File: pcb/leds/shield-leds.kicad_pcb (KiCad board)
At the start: 8 copper layers, 50 x 50 mm, 406 parts, among them J1 QSH-060-01-L-D-A, J2 QSH-060-01-L-D-A, J3 QTH-060-01-L-D-A, J4 QTH-060-01-L-D-A

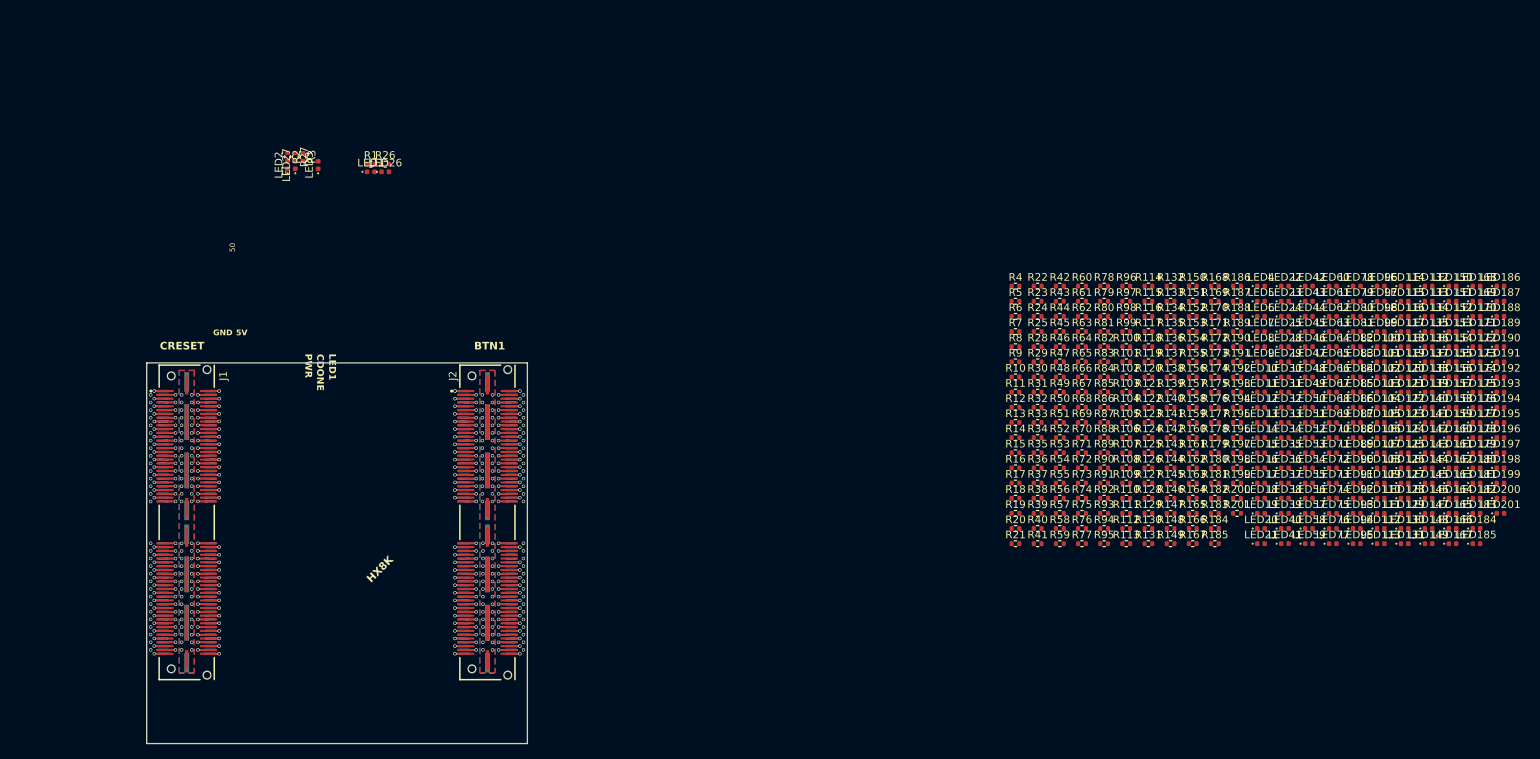
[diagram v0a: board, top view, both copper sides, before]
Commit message: [pcb][leds] left side routed
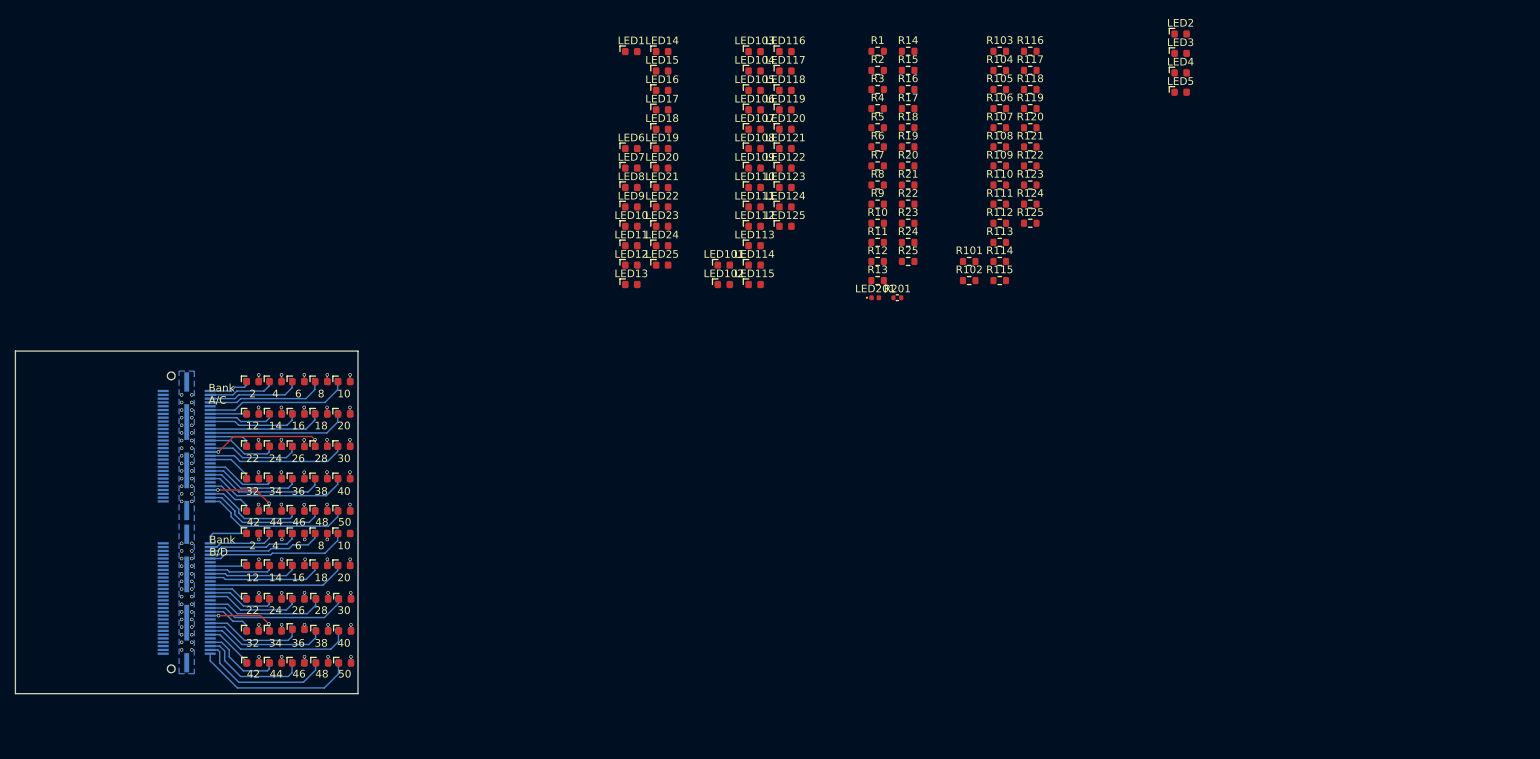
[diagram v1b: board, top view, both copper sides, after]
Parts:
- removed the J1 at (41.8, 81.1)
- removed J2: QSH-060-01-L-D-A, !Misc:SAMTEC_QSH-060-01-X-D-A
- removed J4: QTH-060-01-L-D-A, !Misc:SAMTEC_QTH-060-01-X-D-A
- removed LED100, LED151, LED152, LED153, LED154, LED155, LED156, LED157, LED158, LED159, LED160, LED161, LED162, LED163, LED164, LED165, LED166, LED167, LED168, LED169, LED170, LED171, LED172, LED173, LED174, LED175, LED176, LED177, LED178, LED179, LED180, LED181, LED182, LED183, LED184, LED185, LED186, LED187, LED188, LED189, LED190, LED191, LED192, LED193, LED194, LED195, LED196, LED197, LED198, LED199, LED200, LED51, LED52, LED53, LED54, LED55, LED56, LED57, LED58, LED59, LED60, LED61, LED62, LED63, LED64, LED65, LED66, LED67, LED68, LED69, LED70, LED71, LED72, LED73, LED74, LED75, LED76, LED77, LED78, LED79, LED80, LED81, LED82, LED83, LED84, LED85, LED86, LED87, LED88, LED89, LED90, LED91, LED92, LED93, LED94, LED95, LED96, LED97, LED98, LED99: Blue, Diode_SMD:D_0402_1005Metric
- removed R100, R151, R152, R153, R154, R155, R156, R157, R158, R159, R160, R161, R162, R163, R164, R165, R166, R167, R168, R169, R170, R171, R172, R173, R174, R175, R176, R177, R178, R179, R180, R181, R182, R183, R184, R185, R186, R187, R188, R189, R190, R191, R192, R193, R194, R195, R196, R197, R198, R199, R200, R51, R52, R53, R54, R55, R56, R57, R58, R59, R60, R61, R62, R63, R64, R65, R66, R67, R68, R69, R70, R71, R72, R73, R74, R75, R76, R77, R78, R79, R80, R81, R82, R83, R84, R85, R86, R87, R88, R89, R90, R91, R92, R93, R94, R95, R96, R97, R98, R99: 2.2k, Resistor_SMD:R_0402_1005Metric
- LED1, LED10, LED101, LED102, LED103, LED104, LED105, LED106, LED107, LED108, LED109, LED11, LED110, LED111, LED112, LED113, LED114, LED115, LED116, LED117, LED118, LED119, LED12, LED120, LED121, LED122, LED123, LED124, LED125, LED126, LED127, LED128, LED129, LED13, LED130, LED131, LED132, LED133, LED134, LED135, LED136, LED137, LED138, LED139, LED14, LED140, LED141, LED142, LED143, LED144, LED145, LED146, LED147, LED148, LED149, LED15, LED150, LED16, LED17, LED18, LED19, LED2, LED20, LED21, LED22, LED23, LED24, LED25, LED26, LED27, LED28, LED29, LED3, LED30, LED31, LED32, LED33, LED34, LED35, LED36, LED37, LED38, LED39, LED4, LED40, LED41, LED42, LED43, LED44, LED45, LED46, LED47, LED48, LED49, LED5, LED50, LED6, LED7, LED8, LED9: footprint Diode_SMD:D_0402_1005Metric -> !Misc:D_0603_1608Metric
- R1, R10, R101, R102, R103, R104, R105, R106, R107, R108, R109, R11, R110, R111, R112, R113, R114, R115, R116, R117, R118, R119, R12, R120, R121, R122, R123, R124, R125, R13, R14, R15, R16, R17, R18, R19, R2, R20, R21, R22, R23, R24, R25, R3, R4, R5, R6, R7, R8, R9: footprint Resistor_SMD:R_0402_1005Metric -> Resistor_SMD:R_0603_1608Metric
- R126, R127, R128, R129, R130, R131, R132, R133, R134, R135, R136, R137, R138, R139, R140, R141, R142, R143, R144, R145, R146, R147, R148, R149, R150, R26, R27, R28, R29, R30, R31, R32, R33, R34, R35, R36, R37, R38, R39, R40, R41, R42, R43, R44, R45, R46, R47, R48, R49, R50: footprint Resistor_SMD:R_0402_1005Metric -> Resistor_SMD:R_0603_1608Metric; moved to B.Cu
- moved LED136 158.0 mm to (50.5, 91.2)
- moved LED141 156.9 mm to (50.5, 95.4)
- moved LED146 155.9 mm to (50.5, 99.6)
- moved LED132 155.8 mm to (53.5, 86.8)
- moved LED137 154.6 mm to (53.5, 91.2)
- moved LED150 153.7 mm to (62.6, 99.6)
- moved LED142 153.6 mm to (53.5, 95.4)
- moved LED147 152.7 mm to (53.5, 99.6)
- moved LED133 152.4 mm to (56.5, 86.8)
- moved LED126 151.6 mm to (50.4, 82.5)
- moved LED131 151.3 mm to (50.5, 86.8)
- moved LED138 151.3 mm to (56.5, 91.2)
- moved LED143 150.2 mm to (56.5, 95.1)
- moved LED148 149.5 mm to (56.4, 99.6)
- moved LED134 149.1 mm to (59.5, 86.8)
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- renumbered J3 to J1
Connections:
- R101 pad 1: C1 -> B1
- R102 pad 1: C3 -> B3
- R103 pad 1: C5 -> B5
- R104 pad 1: C7 -> B7
- R105 pad 1: C9 -> B9
- R106 pad 1: C11 -> B11
- R107 pad 1: C13 -> B13
- R108 pad 1: C15 -> B15
- R109 pad 1: C17 -> B17
- R110 pad 1: C19 -> B19
- R111 pad 1: C21 -> B21
- R112 pad 1: C23 -> B23
- R113 pad 1: C25 -> B25
- R114 pad 1: C27 -> B27
- R115 pad 1: C29 -> B29
- R116 pad 1: C31 -> B31
- R117 pad 1: C33 -> B33
- R118 pad 1: C35 -> B35
- R119 pad 1: C37 -> B37
- R120 pad 1: C39 -> B39
- R121 pad 1: C41 -> B41
- R122 pad 1: C43 -> B43
- R123 pad 1: C45 -> B45
- R124 pad 1: C47 -> B47
- R125 pad 1: C49 -> B49
- R126 pad 1: C2 -> B2
- R127 pad 1: C4 -> B4
- R128 pad 1: C6 -> B6
- R129 pad 1: C8 -> B8
- R130 pad 1: C10 -> B10
- R131 pad 1: C12 -> B12
- R132 pad 1: C14 -> B14
- R133 pad 1: C16 -> B16
- R134 pad 1: C18 -> B18
- R135 pad 1: C20 -> B20
- R136 pad 1: C22 -> B22
- R137 pad 1: C24 -> B24
- R138 pad 1: C26 -> B26
- R139 pad 1: C28 -> B28
- R140 pad 1: C30 -> B30
- R141 pad 1: C32 -> B32
- R142 pad 1: C34 -> B34
- R143 pad 1: C36 -> B36
- R144 pad 1: C38 -> B38
- R145 pad 1: C40 -> B40
- R146 pad 1: C42 -> B42
- R147 pad 1: C44 -> B44
- R148 pad 1: C46 -> B46
- R149 pad 1: C48 -> B48
- R150 pad 1: C50 -> B50
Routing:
- net +3V3: track 111.4 -> 0.00 mm, vias 40 -> 0
- net B50: track 3.76 -> 21.5 mm, vias 1 -> 0
- net B30: track 1.18 -> 18.7 mm, vias 1 -> 0
- net A50: track 3.02 -> 19.7 mm, vias 1 -> 0
- net A40: track 3.02 -> 19.1 mm, vias 1 -> 0
- net A10: track 3.02 -> 18.9 mm, vias 1 -> 0
- net B40: track 3.98 -> 19.7 mm, vias 1 -> 0
- net B20: track 2.58 -> 18.2 mm, vias 1 -> 0
- net B10: track 3.02 -> 18.7 mm, vias 1 -> 0
- net A20: track 3.02 -> 18.4 mm, vias 1 -> 0
- net A30: track 3.02 -> 18.3 mm, vias 1 -> 0
- net B48: track 3.02 -> 18.1 mm, vias 1 -> 0
- net A48: track 2.58 -> 16.4 mm, vias 1 -> 0
- net A38: track 2.58 -> 15.9 mm, vias 1 -> 0
- net A28: track 2.58 -> 15.7 mm, vias 1 -> 2
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- removed copper zone on F.Cu, net GND
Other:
- board size 50 x 50 mm -> 45 x 45 mm
- board text added: "10"
- board text added: "12"
- board text added: "14"
- board text added: "16"
- board text added: "18"
- board text added: "2"
- board text added: "20"
- board text added: "22"
- board text added: "24"
- board text added: "26"
- board text added: "28"
- board text added: "30"
- board text added: "32"
- board text added: "34"
- board text added: "36"
- board text added: "38"
- board text added: "4"
- board text added: "40"
- board text added: "42"
- board text added: "44"
- board text added: "46"
- board text added: "48"
- board text added: "6"
- board text added: "8"
- board text added: "Bank A/C"
- board text added: "Bank B/D"
- board text removed: "100 Mhz"
- board text removed: "1V2"
- board text removed: "3V3"
- board text removed: "5V"
- board text removed: "BTN1"
- board text removed: "CDONE"
- board text removed: "CRESET"
- board text removed: "GND"
- board text removed: "HX8K"
- board text removed: "LED1"
- board text removed: "PWR"

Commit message: [pcb][leds] fully routed
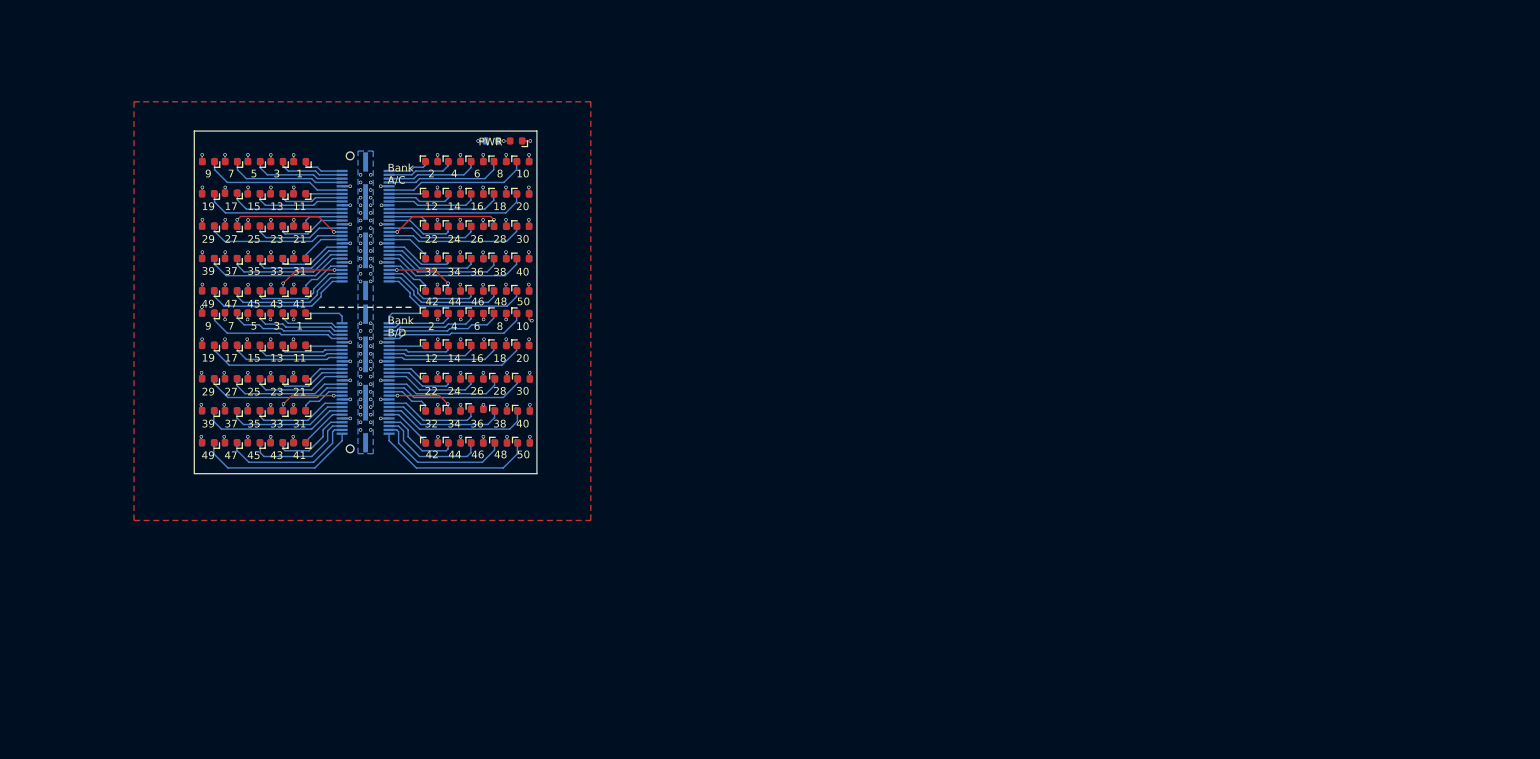
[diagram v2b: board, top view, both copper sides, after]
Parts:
- LED201: footprint Diode_SMD:D_0402_1005Metric -> !Misc:D_0603_1608Metric
- R1, R10, R101, R102, R103, R104, R105, R106, R107, R108, R109, R11, R110, R111, R112, R113, R114, R115, R116, R117, R118, R119, R12, R120, R121, R122, R123, R124, R125, R13, R14, R15, R16, R17, R18, R19, R2, R20, R21, R22, R23, R24, R25, R3, R4, R5, R6, R7, R8, R9: moved to B.Cu
- R201: footprint Resistor_SMD:R_0402_1005Metric -> Resistor_SMD:R_0603_1608Metric; moved to B.Cu
- moved LED5 128.0 mm to (44.6, 33.7), turned to 180 degrees
- moved LED4 125.2 mm to (47.6, 33.7), turned to 180 degrees
- moved LED3 122.5 mm to (50.6, 33.7), turned to 180 degrees
- moved LED2 119.9 mm to (53.6, 33.7), turned to 180 degrees
- moved R120 114.2 mm to (44.6, 66.4), turned to 180 degrees
- moved R119 112.2 mm to (47.6, 66.4), turned to 180 degrees
- moved R125 111.8 mm to (44.6, 70.6), turned to 180 degrees
- moved R118 110.4 mm to (50.6, 66.4), turned to 180 degrees
- moved R124 109.5 mm to (47.6, 70.6), turned to 180 degrees
- moved R117 108.6 mm to (53.6, 66.4), turned to 180 degrees
- moved R105 108.0 mm to (44.6, 53.6), turned to 180 degrees
- moved R123 107.4 mm to (50.6, 70.6), turned to 180 degrees
- moved R116 107.0 mm to (56.6, 66.4), turned to 180 degrees
- moved R110 106.1 mm to (44.6, 57.8), turned to 180 degrees
- moved R104 105.9 mm to (47.6, 53.6), turned to 180 degrees
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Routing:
- net +3V3: track 0.00 -> 22.9 mm, vias 0 -> 21
- net B49: track 0.00 -> 21.5 mm
- net B39: track 0.00 -> 19.7 mm
- net A49: track 0.00 -> 19.7 mm
- net A39: track 0.00 -> 19.1 mm
- net A9: track 0.00 -> 18.9 mm
- net B29: track 0.00 -> 18.7 mm
- net B9: track 0.00 -> 18.7 mm
- net A19: track 0.00 -> 18.4 mm
- net A29: track 0.00 -> 18.3 mm
- net B19: track 0.00 -> 18.2 mm
- net B47: track 0.00 -> 18.1 mm
- net A47: track 0.00 -> 16.4 mm
- net B37: track 0.00 -> 16.1 mm
- net A37: track 0.00 -> 15.9 mm
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- added copper zone on In2.Cu, net +3V3
- added copper zone on F.Cu, net GND
- removed copper zone on In3.Cu, net +3V3
- removed copper zone on In4.Cu, net GND
- removed copper zone on In6.Cu, net GND
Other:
- copper layers 8 -> 4
- board text added: "1"
- board text added: "11"
- board text added: "13"
- board text added: "15"
- board text added: "17"
- board text added: "19"
- board text added: "21"
- board text added: "23"
- board text added: "25"
- board text added: "27"
- board text added: "29"
- board text added: "3"
- board text added: "31"
- board text added: "33"
- board text added: "35"
- board text added: "37"
- board text added: "39"
- board text added: "41"
- board text added: "43"
- board text added: "45"
- board text added: "47"
- board text added: "49"
- board text added: "5"
- board text added: "7"
- board text added: "9"
- board text added: "PWR"
- board text added: "v1.0"
